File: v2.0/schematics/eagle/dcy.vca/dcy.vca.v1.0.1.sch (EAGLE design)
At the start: 28 parts, among them IC1 LM324N, IC2 4001N, IC3 LM324N, IC4 TL074P

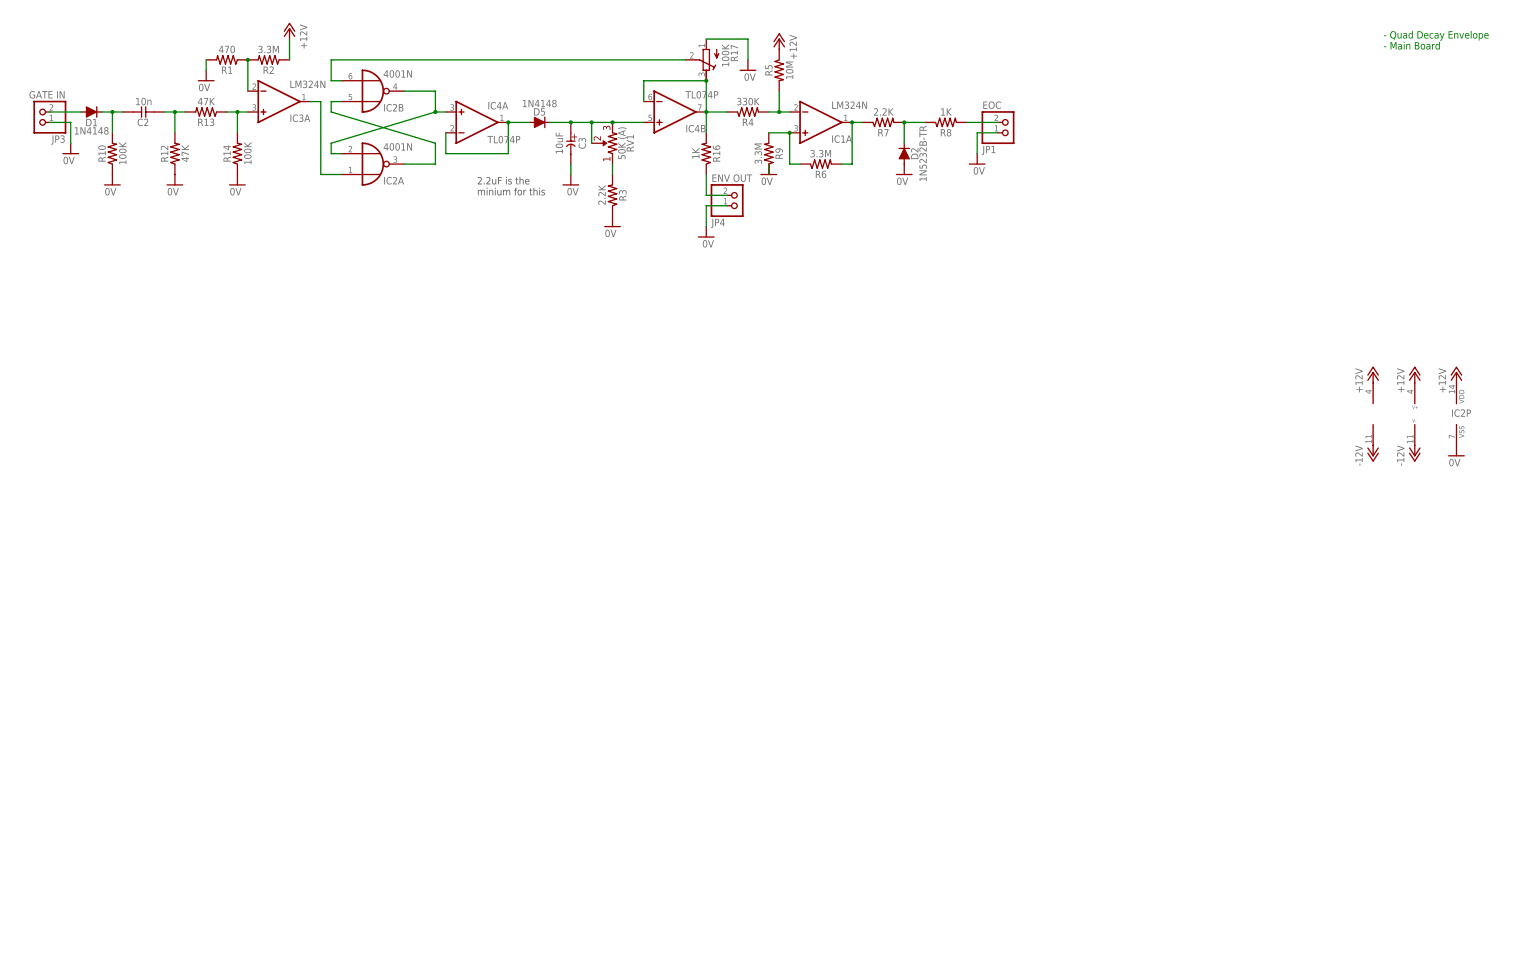
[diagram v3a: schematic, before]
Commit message: Updated diode packages and zenner symbol
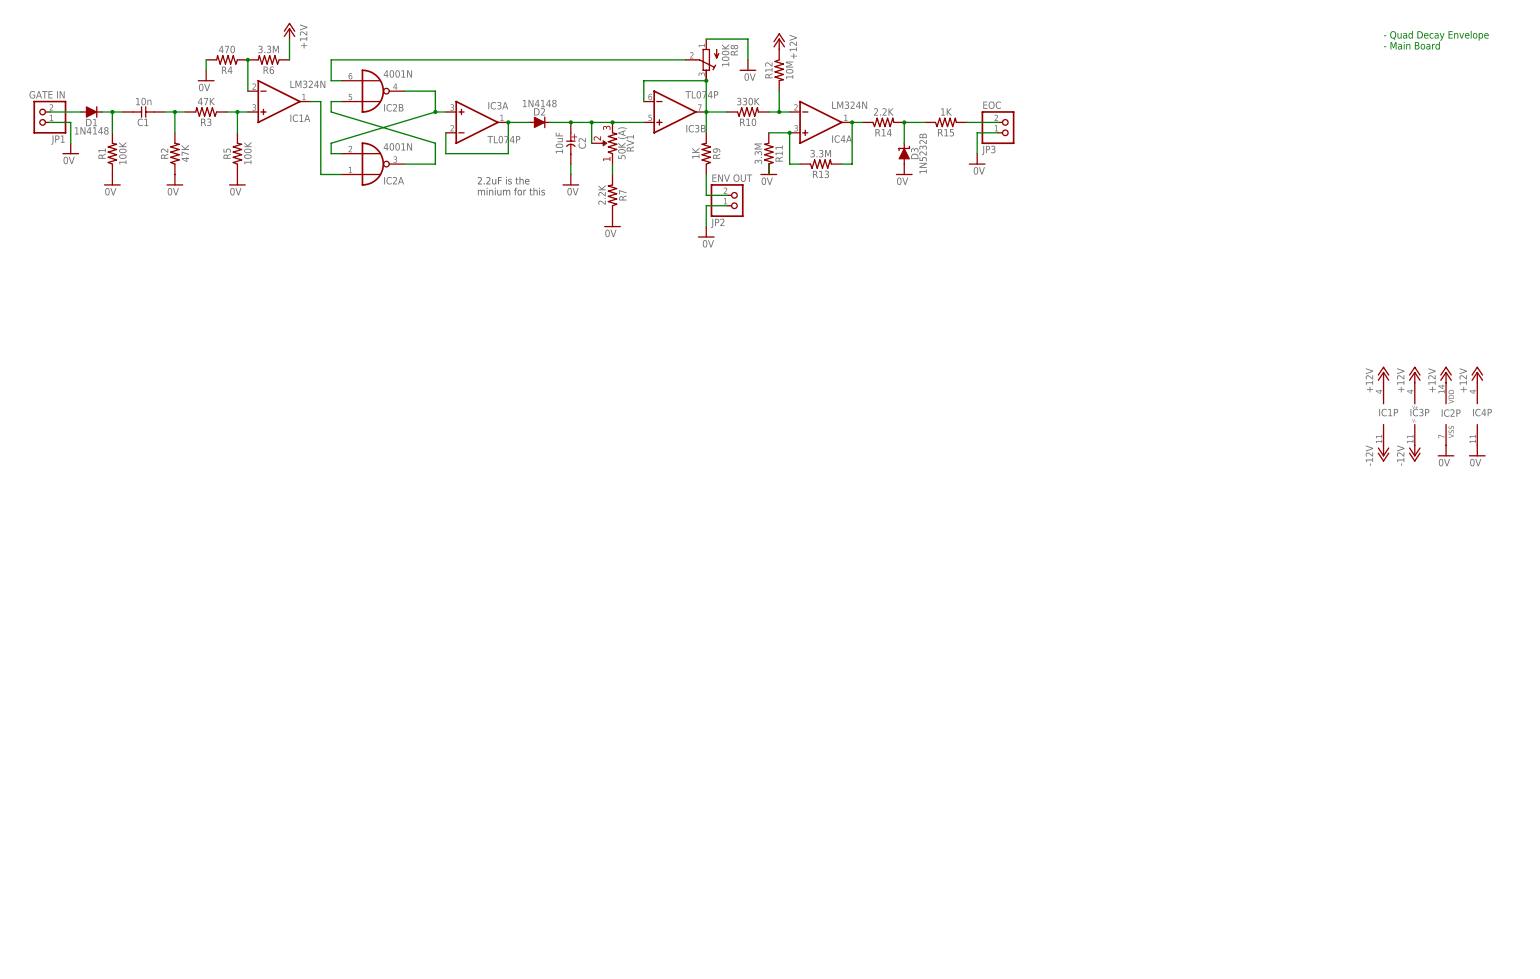
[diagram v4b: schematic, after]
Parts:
- removed C3: 10uF, _common:CE-USE2-5
- removed D5: 1N4148, _common:1N4148
- removed R16: 1K, _common:R0309/10
- removed R17: 100K, rcl:R-TRIMM3339P
- added C1: 10n, _common:CC-US025-024X044
- added D3: 1N5232B, _common:1N5232B
- added R11: 3.3M, _common:R0309/10
- added R15: 1K, _common:R0309/10
- C2: value 10n -> 10uF; device _common:CC-US025-024X044 -> _common:CE-USE2-5
- D2: value 1N5232B-TR -> 1N4148; device _common:1N5232B-TR -> _common:1N4148
- IC3: value LM324N -> TL074P; device linear:LM324N -> _common:TL074P
- IC4: value TL074P -> LM324N; device _common:TL074P -> linear:LM324N
- JP1: value EOC -> GATE IN
- JP3: value GATE IN -> EOC
- R1: value 470 -> 100K
- R10: value 100K -> 330K
- R12: value 47K -> 10M
- R13: value 47K -> 3.3M
- R14: value 100K -> 2.2K
- R2: value 3.3M -> 47K
- R3: value 2.2K -> 47K
- R4: value 330K -> 470
- R5: value 10M -> 100K
- R8: value 1K -> 100K; device _common:R0309/10 -> rcl:R-TRIMM3339P
- R9: value 3.3M -> 1K
- renumbered JP4 to JP2
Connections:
- net +12V: now also IC1P.V+, R12.1, R6.1; no longer R2.1, R5.1
- net -12V: now also IC1P.V-; no longer IC4P.V-
- net 0V: now also C2.-, D3.A, IC4P.V-, R1.1, R11.1, R2.1, R4.2, R5.1, R7.1, R8.A; no longer C3.-, D2.A, R1.2, R10.1, R12.1, R14.1, R17.A, R3.1, R9.1
- net N$1: now also R7.2; no longer R3.2
- net N$14: now also IC3A.+IN; no longer IC4A.+IN
- net N$15: now also JP1.2; no longer JP3.2
- net N$17: now also D2.A, IC3A.-IN, IC3A.OUT; no longer D5.A, IC4A.-IN, IC4A.OUT
- net N$18: now also C1.1, R1.2; no longer C2.1, R10.2
- net N$19: now also C1.2, R2.2, R3.2; no longer C2.2, R12.2, R13.2
- net N$2: now also IC4A.-IN, R10.2, R12.2; no longer IC1A.-IN, R4.2, R5.2
- net N$20: now also IC1A.+IN, R3.1, R5.2; no longer IC3A.+IN, R13.1, R14.2
- net N$21: now also IC1A.-IN, R4.1, R6.2; no longer IC3A.-IN, R1.1, R2.2
- net N$22: now also IC1A.OUT; no longer IC3A.OUT
- net N$23: now also IC3B.-IN, IC3B.OUT, R10.1, R8.E, R9.2; no longer IC4B.-IN, IC4B.OUT, R16.2, R17.E, R4.1
- net N$24: now also R9.1; no longer R16.1
- net N$25: now also R8.S; no longer R17.S
- net N$3: now also IC4A.+IN, R11.2, R13.1; no longer IC1A.+IN, R6.1, R9.2
- net N$5: now also IC4A.OUT, R13.2, R14.1; no longer IC1A.OUT, R6.2, R7.1
- net N$6: now also D3.C, R14.2, R15.1; no longer D2.C, R7.2, R8.1
- net N$63: now also C2.+, D2.C, IC3B.+IN; no longer C3.+, D5.C, IC4B.+IN
- net N$7: now also JP3.2, R15.2; no longer JP1.2, R8.2
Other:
- moved on the sheet: C2, D2, IC1A, IC2P, IC3A, IC4A, JP1, JP3, R1, R10, R12, R13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

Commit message: Duplicated main schem (x4)
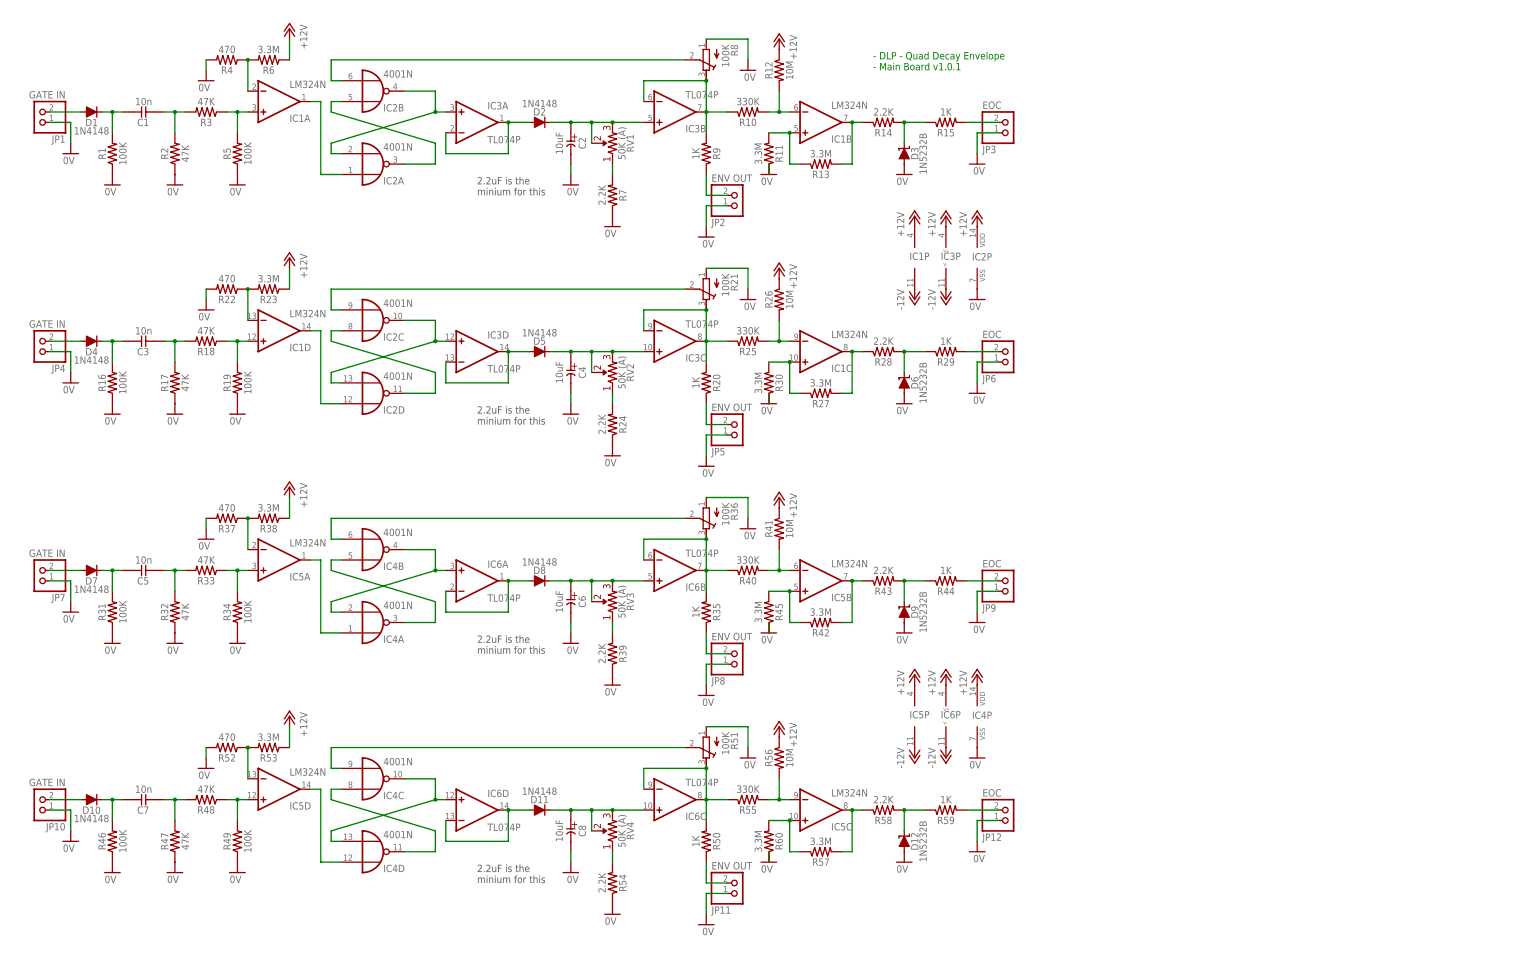
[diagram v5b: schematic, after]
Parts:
- added C3, C5, C7: 10n, _common:CC-US025-024X044
- added C4, C6, C8: 10uF, _common:CE-USE2-5
- added D10, D11, D4, D5, D7, D8: 1N4148, _common:1N4148
- added D12, D6, D9: 1N5232B, _common:1N5232B
- added IC5: LM324N, linear:LM324N
- added IC6: TL074P, _common:TL074P
- added JP10, JP4, JP7: GATE IN, pinhead:PINHD-1X2
- added JP11, JP5, JP8: ENV OUT, pinhead:PINHD-1X2
- added JP12, JP6, JP9: EOC, pinhead:PINHD-1X2
- added R16, R19, R31, R34, R46, R49: 100K, _common:R0309/10
- added R17, R18, R32, R33, R47, R48: 47K, _common:R0309/10
- added R20, R29, R35, R44, R50, R59: 1K, _common:R0309/10
- added R21, R36, R51: 100K, rcl:R-TRIMM3339P
- added R22, R37, R52: 470, _common:R0309/10
- added R23, R27, R30, R38, R42, R45, R53, R57, R60: 3.3M, _common:R0309/10
- added R24, R28, R39, R43, R54, R58: 2.2K, _common:R0309/10
- added R25, R40, R55: 330K, _common:R0309/10
- added R26, R41, R56: 10M, _common:R0309/10
- added RV2, RV3, RV4: 50K (A), _common:R-VAR
- IC4: value LM324N -> 4001N; device linear:LM324N -> 40xx:4001N
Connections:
- new net N$10: D4.A, JP4.2
- new net N$11: C3.1, D4.C, R16.2
- new net N$12: C3.2, R17.2, R18.2
- new net N$13: IC1D.+IN, R18.1, R19.2
- new net N$16: IC1D.-IN, R22.1, R23.2
- new net N$26: IC1D.OUT, IC2D.I0
- new net N$27: D5.A, IC3D.-IN, IC3D.OUT
- new net N$28: IC3C.-IN, IC3C.OUT, R20.2, R21.E, R25.1
- new net N$29: JP5.2, R20.1
- new net N$30: IC2C.I1, R21.S
- new net N$31: C4.+, D5.C, IC3C.+IN, RV2.2, RV2.P$1
- new net N$32: R24.2, RV2.1
- new net N$33: IC1C.-IN, R25.2, R26.2
- new net N$34: IC1C.+IN, R27.1, R30.2
- new net N$35: IC1C.OUT, R27.2, R28.1
- new net N$36: D6.C, R28.2, R29.1
- new net N$37: JP6.2, R29.2
- new net N$38: IC4A.O, IC4B.I0
- new net N$39: IC4A.I1, IC4B.O, IC6A.+IN
- new net N$40: D7.A, JP7.2
- new net N$41: C5.1, D7.C, R31.2
- new net N$42: C5.2, R32.2, R33.2
- new net N$43: IC5A.+IN, R33.1, R34.2
- new net N$44: IC5A.-IN, R37.1, R38.2
- new net N$45: IC4A.I0, IC5A.OUT
- new net N$46: D8.A, IC6A.-IN, IC6A.OUT
- new net N$47: IC6B.-IN, IC6B.OUT, R35.2, R36.E, R40.1
- new net N$48: JP8.2, R35.1
- new net N$49: IC4B.I1, R36.S
- new net N$50: C6.+, D8.C, IC6B.+IN, RV3.2, RV3.P$1
- new net N$51: R39.2, RV3.1
- new net N$52: IC5B.-IN, R40.2, R41.2
- new net N$53: IC5B.+IN, R42.1, R45.2
- new net N$54: IC5B.OUT, R42.2, R43.1
- new net N$55: D9.C, R43.2, R44.1
- new net N$56: JP9.2, R44.2
- new net N$57: IC4C.I0, IC4D.O
- new net N$58: IC4C.O, IC4D.I1, IC6D.+IN
- new net N$59: D10.A, JP10.2
- new net N$60: C7.1, D10.C, R46.2
- new net N$61: C7.2, R47.2, R48.2
- new net N$62: IC5D.+IN, R48.1, R49.2
- new net N$64: IC5D.-IN, R52.1, R53.2
- new net N$65: IC4D.I0, IC5D.OUT
- new net N$66: D11.A, IC6D.-IN, IC6D.OUT
- new net N$67: IC6C.-IN, IC6C.OUT, R50.2, R51.E, R55.1
- new net N$68: JP11.2, R50.1
- new net N$69: IC4C.I1, R51.S
- new net N$70: C8.+, D11.C, IC6C.+IN, RV4.2, RV4.P$1
- new net N$71: R54.2, RV4.1
- new net N$72: IC5C.-IN, R55.2, R56.2
- new net N$73: IC5C.+IN, R57.1, R60.2
- new net N$74: IC5C.OUT, R57.2, R58.1
- new net N$75: D12.C, R58.2, R59.1
- new net N$76: JP12.2, R59.2
- new net N$8: IC2C.I0, IC2D.O
- new net N$9: IC2C.O, IC2D.I1, IC3D.+IN
- net +12V: now also IC4P.VDD, IC5P.V+, IC6P.V+, R23.1, R26.1, R38.1, R41.1, R53.1, R56.1; no longer IC4P.V+
- net -12V: now also IC5P.V-, IC6P.V-
- net 0V: now also C4.-, C6.-, C8.-, D12.A, D6.A, D9.A, IC4P.VSS, JP10.1, JP11.1, JP12.1, JP4.1, JP5.1, JP6.1, JP7.1, JP8.1, JP9.1, R16.1, R17.1, R19.1, R21.A, R22.2, R24.1, R30.1, R31.1, R32.1, R34.1, R36.A, R37.2, R39.1, R45.1, R46.1, R47.1, R49.1, R51.A, R52.2, R54.1, R60.1; no longer IC4P.V-
- net N$2: now also IC1B.-IN; no longer IC4A.-IN
- net N$3: now also IC1B.+IN; no longer IC4A.+IN
- net N$5: now also IC1B.OUT; no longer IC4A.OUT
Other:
- note added: "- DLP - Quad Decay Envelope - Main Board v1.0.1"
- note removed: "- Quad Decay Envelope - Main Board"
- moved on the sheet: IC1P, IC2P, IC3P

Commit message: Completed layout of main board for quad decay
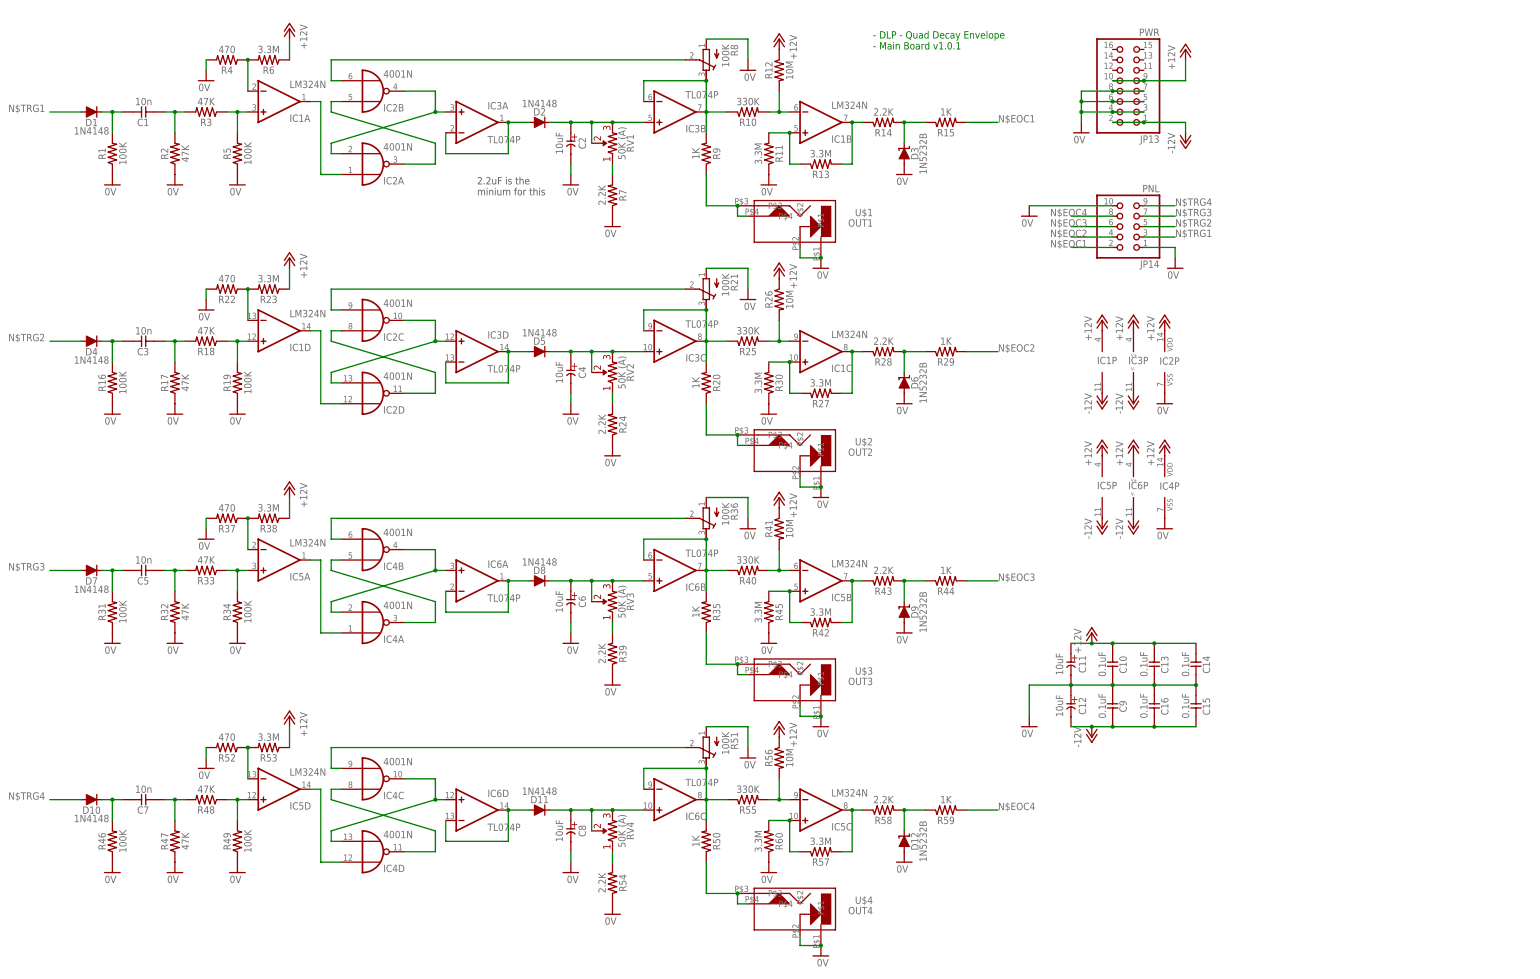
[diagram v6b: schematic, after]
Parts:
- removed JP1, JP10, JP4, JP7: GATE IN, pinhead:PINHD-1X2
- removed JP11, JP2, JP5, JP8: ENV OUT, pinhead:PINHD-1X2
- removed JP12, JP3, JP6, JP9: EOC, pinhead:PINHD-1X2
- added C10, C13, C14, C15, C16, C9: 0.1uF, _common:CC-US025-024X044
- added C11, C12: 10uF, _common:CE-USE2-5
- added JP13: PWR, pinhead:PINHD-2X8
- added JP14: PNL, pinhead:PINHD-2X5
- added U$1: OUT1, jacks:CL1384
- added U$2: OUT2, jacks:CL1384
- added U$3: OUT3, jacks:CL1384
- added U$4: OUT4, jacks:CL1384
- R1, R10, R11, R12, R13, R14, R15, R16, R17, R18, R19, R2, R20, R22, R23, R24, R25, R26, R27, R28, R29, R3, R30, R31, R32, R33, R34, R35, R37, R38, R39, R4, R40, R41, R42, R43, R44, R45, R46, R47, R48, R49, R5, R50, R52, R53, R54, R55, R56, R57, R58, R59, R6, R60, R7, R9: device _common:R0309/10 -> _common:R
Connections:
- removed net N$10: D4.A, JP4.2
- removed net N$15: D1.A, JP1.2
- removed net N$37: JP6.2, R29.2
- removed net N$40: D7.A, JP7.2
- removed net N$56: JP9.2, R44.2
- removed net N$59: D10.A, JP10.2
- removed net N$7: JP3.2, R15.2
- removed net N$76: JP12.2, R59.2
- new net N$EOC1: JP14.2, R15.2
- new net N$EOC2: JP14.4, R29.2
- new net N$EOC3: JP14.6, R44.2
- new net N$EOC4: JP14.8, R59.2
- new net N$TRG1: D1.A, JP14.3
- new net N$TRG2: D4.A, JP14.5
- new net N$TRG3: D7.A, JP14.7
- new net N$TRG4: D10.A, JP14.9
- net +12V: now also C10.2, C11.+, C13.2, C14.2, JP13.10, JP13.9
- net -12V: now also C12.-, C15.1, C16.1, C9.1, JP13.1, JP13.2
- net 0V: now also C10.1, C11.-, C12.+, C13.1, C14.1, C15.2, C16.2, C9.2, JP13.3, JP13.4, JP13.5, JP13.6, JP13.7, JP13.8, JP14.1, JP14.10, U$1.P$1, U$1.P$2, U$2.P$1, U$2.P$2, U$3.P$1, U$3.P$2, U$4.P$1, U$4.P$2; no longer JP1.1, JP10.1, JP11.1, JP12.1, JP2.1, JP3.1, JP4.1, JP5.1, JP6.1, JP7.1, JP8.1, JP9.1
- net N$24: now also U$1.P$3, U$1.P$4; no longer JP2.2
- net N$29: now also U$2.P$3, U$2.P$4; no longer JP5.2
- net N$48: now also U$3.P$3, U$3.P$4; no longer JP8.2
- net N$68: now also U$4.P$3, U$4.P$4; no longer JP11.2
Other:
- moved on the sheet: IC1P, IC2P, IC3P, IC4P, IC5P, IC6P
